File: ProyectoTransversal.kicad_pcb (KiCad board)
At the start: 2 copper layers, 20 parts, among them J1 Conn_01x19, J2 Conn_01x19, J3 Screw_Terminal_01x02, J4 Screw_Terminal_01x02, J5 Conn_01x04, K1 Relay_SPDT, Q1 IRLZ44N, Q2 BC547, U1 DS18B20, U2 LM2596S-5

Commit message: Route voltage regulator
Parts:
- J5: footprint Connector_PinHeader_2.54mm:PinHeader_1x19_P2.54mm_Vertical -> Connector_PinHeader_2.54mm:PinHeader_1x04_P2.54mm_Vertical
- moved J3 317.3 mm to (270.5, 107.5)
- moved J1 289.8 mm to (166.8, 73.9)
- moved J4 262.2 mm to (218.7, 70.8), turned to -90 degrees
- moved C1 261.7 mm to (205.7, 71.5), turned to -90 degrees
- moved J2 254.1 mm to (144.0, 73.9)
- moved U2 251.5 mm to (196.2, 70.9), turned to -90 degrees
- moved D2 231.0 mm to (188.2, 68.2), turned to -90 degrees
- moved L1 221.2 mm to (180.2, 73.8), turned to 180 degrees
- moved C2 200.3 mm to (175.2, 63.3), turned to 90 degrees
- moved U1 122.0 mm to (-121.0, 108.9)
- moved J5 108.4 mm to (-133.0, 97.5)
- moved R3 94.0 mm to (-123.8, 100.0)
- moved HS1 78.4 mm to (-46.0, 109.5)
- moved R4 76.7 mm to (-43.1, 2.00)
- moved Q2 70.8 mm to (-40.8, -17.1)
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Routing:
- net GND: track 0.00 -> 106.6 mm
- net /V_reg: track 0.00 -> 52.2 mm
- net /12V: track 0.00 -> 24.5 mm
- net Net-(D2-K): track 0.00 -> 20.2 mm

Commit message: Finish layout
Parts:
- moved R3 299.7 mm to (173.6, 137.5), turned to 180 degrees
- moved J5 290.7 mm to (154.6, 139.5)
- moved U1 290.7 mm to (166.6, 150.9)
- moved Q2 186.5 mm to (117.5, 81.5)
- moved R4 183.4 mm to (118.3, 89.0)
- moved J3 182.7 mm to (88.0, 117.0)
- moved D1 171.7 mm to (99.3, 81.5)
- moved R2 158.7 mm to (134.5, 117.4), turned to -90 degrees
- moved HS1 157.0 mm to (106.8, 145.5)
- moved R1 154.9 mm to (130.6, 117.5), turned to 180 degrees
- moved K1 133.3 mm to (84.0, 56.5)
- moved Q1 128.5 mm to (104.9, 117.5)
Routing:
- net GND: track 106.6 -> 341.2 mm
- net /V_reg: track 52.2 -> 174.8 mm
- net /12V: track 24.5 -> 126.0 mm
- net /Alim_12V: track 0.00 -> 81.0 mm
- net /sensor_temp: track 0.00 -> 61.6 mm
- net /3V3: track 0.00 -> 52.6 mm, vias 0 -> 1
- net /SDA: track 0.00 -> 39.5 mm
- net Net-(D1-A): track 0.00 -> 39.3 mm
- net /SCL: track 0.00 -> 34.4 mm
- net Net-(J3-Pin_1): track 0.00 -> 25.6 mm
- net /GATE: track 0.00 -> 22.7 mm
- net /CMD_Relay: track 0.00 -> 15.6 mm
- net /PWM_OUT: track 0.00 -> 13.6 mm
- net Net-(Q2-B): track 0.00 -> 7.66 mm

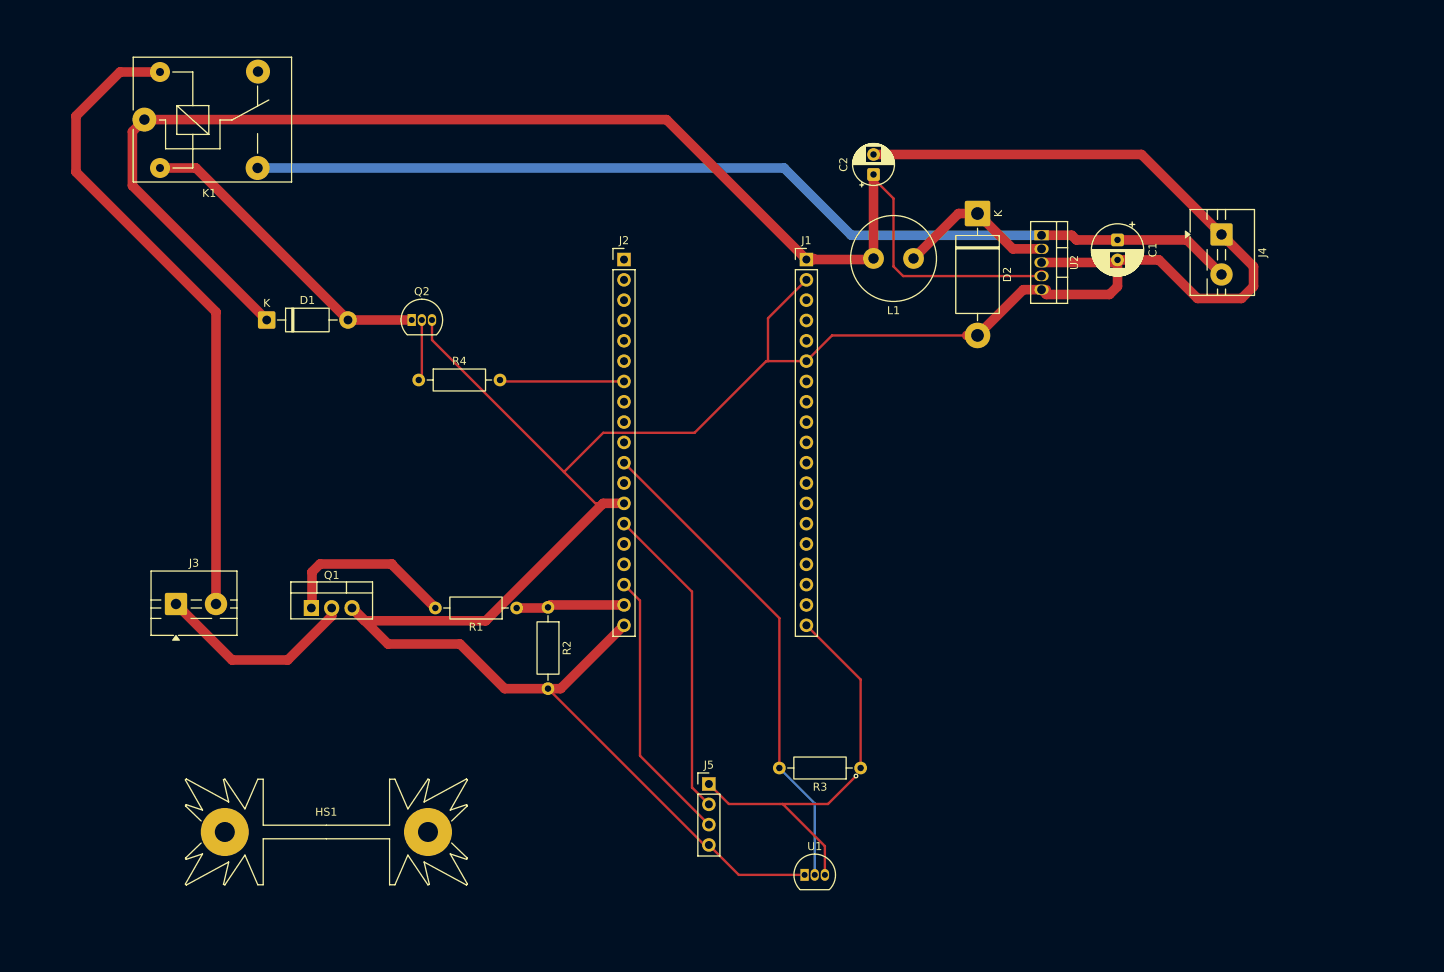
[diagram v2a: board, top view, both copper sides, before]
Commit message: Add copper GND zone
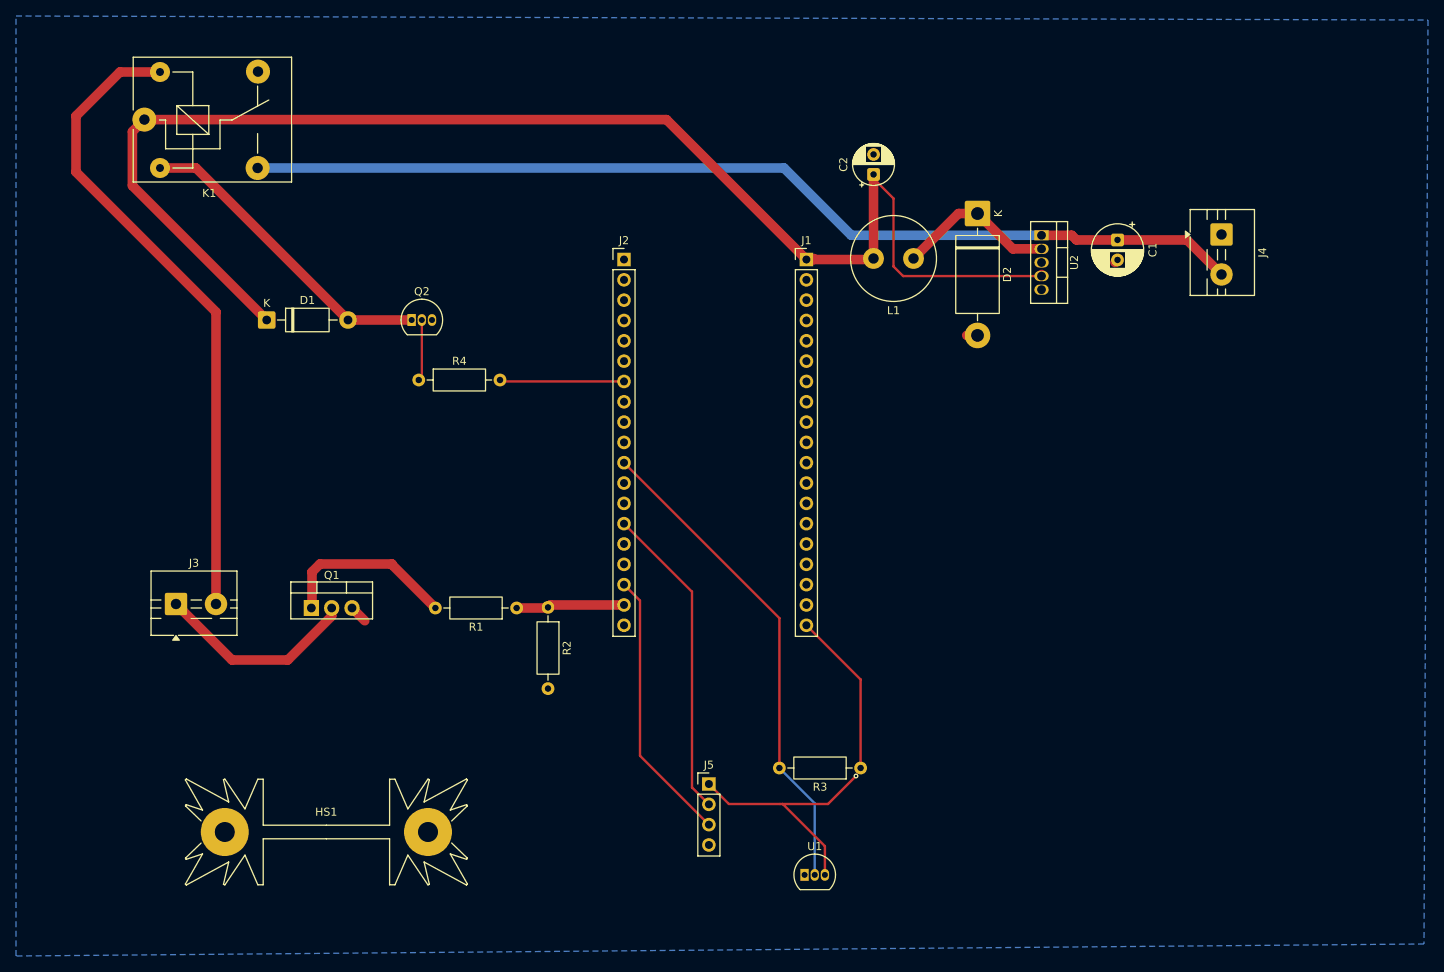
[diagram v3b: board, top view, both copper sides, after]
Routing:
- net GND: track 341.2 -> 5.13 mm
- added copper zone on B.Cu, net GND

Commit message: Delete traces
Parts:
- moved J5 266.1 mm to (-106.0, 85.9)
- moved R3 266.1 mm to (-87.0, 83.9)
- moved U1 266.1 mm to (-94.0, 97.2)
- moved J1 258.7 mm to (-86.7, 22.2)
- moved J2 258.7 mm to (-109.5, 22.2)
- moved C1 238.1 mm to (-31.5, 93.2)
- moved C2 238.1 mm to (-62.0, 85.0)
- moved D2 238.1 mm to (-49.0, 89.9)
- moved J4 238.1 mm to (-18.5, 92.5)
- moved L1 238.1 mm to (-57.0, 95.5)
- moved U2 238.1 mm to (-41.0, 92.6)
- moved R4 172.4 mm to (-41.9, 25.1)
- moved HS1 169.3 mm to (-40.5, 62.1)
- moved J3 165.5 mm to (-60.0, 43.0)
- moved Q1 165.5 mm to (-43.1, 43.5)
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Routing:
- net /V_reg: track 174.8 -> 0.00 mm
- net /12V: track 126.0 -> 0.00 mm
- net /Alim_12V: track 81.0 -> 0.00 mm
- net /sensor_temp: track 61.6 -> 0.00 mm
- net /3V3: track 52.6 -> 0.00 mm
- net /SDA: track 39.5 -> 0.00 mm
- net Net-(D1-A): track 39.3 -> 0.00 mm
- net /SCL: track 34.4 -> 0.00 mm
- net Net-(J3-Pin_1): track 25.6 -> 0.00 mm
- net /GATE: track 22.7 -> 0.00 mm
- net Net-(D2-K): track 20.2 -> 0.00 mm
- net /CMD_Relay: track 15.6 -> 0.00 mm
- net /PWM_OUT: track 13.6 -> 0.00 mm
- net Net-(Q2-B): track 7.66 -> 0.00 mm
- net GND: track 5.13 -> 0.00 mm
- removed copper zone on B.Cu, net GND
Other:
- board outline added: 113.5 x 112.1 mm
